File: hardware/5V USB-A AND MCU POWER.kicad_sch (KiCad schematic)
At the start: 19 parts, among them U2 LMR14050-Q1, U3 NCP177BMX330TCG, U4 NCP177AMX120TCG

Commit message: making hardware progress
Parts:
- added R9: 1.5mR, symbol Device:R
- renumbered C13 to C10, C12 to C11, C14 to C12, C15 to C13, C10 to C14, C11 to C15, C18 to C16, C16 to C17, C19 to C18, C17 to C19, R12 to R11, R8 to R12, R9 to R13, U4 to U3, U3 to U4
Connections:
- net +5V: now also R9.2; no longer C15.1, L2.2, R13.2
- new net 5V_CSN: C15.1, L2.2, R13.2, R9.1

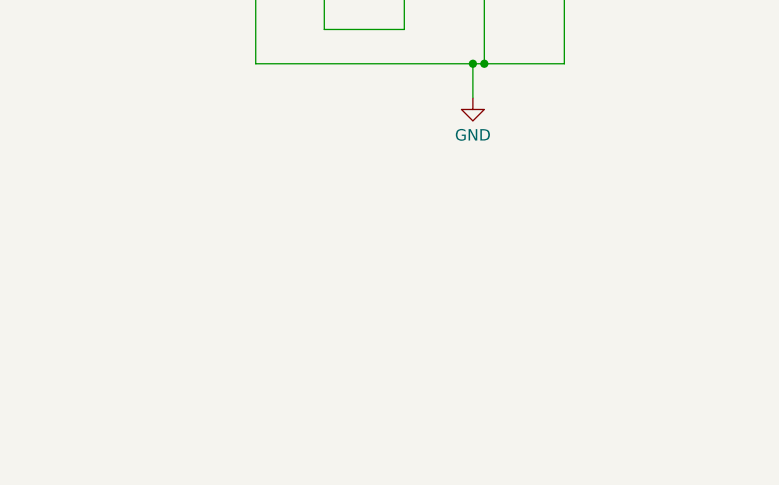
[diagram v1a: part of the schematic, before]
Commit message: working on usb side implimentaion
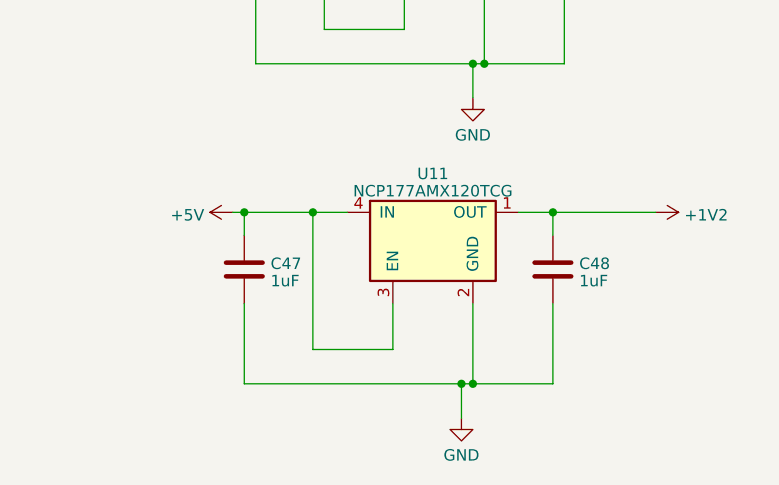
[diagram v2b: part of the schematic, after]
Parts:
- added C47, C48: 1uF, symbol Device:C
- added U11: NCP177AMX120TCG, symbol CARTHING:NCP177BMX330TCG-Regulator_Linear
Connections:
- net +1V2: now also C48.1, U11.1 (OUT)
- net +5V: now also C47.1, U11.3 (EN), U11.4 (IN)
- net GND: now also C47.2, C48.2, U11.2 (GND)
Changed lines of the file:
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@@
   (junction (at 218.44 72.39) (diameter 0) (color 0 0 0 0)
   )
+  (junction (at 182.88 107.95) (diameter 0) (color 0 0 0 0)
+  )
   (junction (at 77.47 88.9) (diameter 0) (color 0 0 0 0)
   )
@@
   (junction (at 135.89 68.58) (diameter 0) (color 0 0 0 0)
   )
+  (junction (at 190.5 107.95) (diameter 0) (color 0 0 0 0)
+  )
   (junction (at 77.47 34.29) (diameter 0) (color 0 0 0 0)
   )
@@
   (junction (at 209.55 91.44) (diameter 0) (color 0 0 0 0)
   )
+  (junction (at 208.28 127) (diameter 0) (color 0 0 0 0)
+  )
+  (junction (at 207.01 127) (diameter 0) (color 0 0 0 0)
+  )
+  (junction (at 217.17 107.95) (diameter 0) (color 0 0 0 0)
+  )
   (junction (at 185.42 31.75) (diameter 0) (color 0 0 0 0)
   )
@@
     (stroke (width 0) (type default))
   )
+  (wire (pts (xy 217.17 107.95) (xy 228.6 107.95))
+    (stroke (width 0) (type default))
+  )
   (wire (pts (xy 77.47 88.9) (xy 77.47 91.44))
     (stroke (width 0) (type default))
@@
     (stroke (width 0) (type default))
   )
+  (wire (pts (xy 190.5 107.95) (xy 194.31 107.95))
+    (stroke (width 0) (type default))
+  )
   (wire (pts (xy 77.47 88.9) (xy 85.09 88.9))
     (stroke (width 0) (type default))
@@
     (stroke (width 0) (type default))
   )
+  (wire (pts (xy 199.39 123.19) (xy 190.5 123.19))
+    (stroke (width 0) (type default))
+  )
   (wire (pts (xy 49.53 88.9) (xy 62.23 88.9))
     (stroke (width 0) (type default))
@@
     (stroke (width 0) (type default))
   )
+  (wire (pts (xy 190.5 123.19) (xy 190.5 107.95))
+    (stroke (width 0) (type default))
+  )
   (wire (pts (xy 110.49 80.01) (xy 110.49 82.55))
     (stroke (width 0) (type default))
@@
     (stroke (width 0) (type default))
   )
+  (wire (pts (xy 199.39 118.11) (xy 199.39 123.19))
+    (stroke (width 0) (type default))
+  )
   (wire (pts (xy 185.42 50.8) (xy 209.55 50.8))
     (stroke (width 0) (type default))
   )
+  (wire (pts (xy 208.28 127) (xy 207.01 127))
+    (stroke (width 0) (type default))
+  )
+  (wire (pts (xy 217.17 118.11) (xy 217.17 127))
+    (stroke (width 0) (type default))
+  )
+  (wire (pts (xy 217.17 107.95) (xy 217.17 110.49))
+    (stroke (width 0) (type default))
+  )
   (wire (pts (xy 102.87 80.01) (xy 110.49 80.01))
     (stroke (width 0) (type default))
@@
     (stroke (width 0) (type default))
   )
+  (wire (pts (xy 181.61 107.95) (xy 182.88 107.95))
+    (stroke (width 0) (type default))
+  )
   (wire (pts (xy 193.04 31.75) (xy 196.85 31.75))
     (stroke (width 0) (type default))
@@
     (stroke (width 0) (type default))
   )
+  (wire (pts (xy 208.28 118.11) (xy 208.28 127))
+    (stroke (width 0) (type default))
+  )
   (wire (pts (xy 77.47 50.8) (xy 76.2 50.8))
     (stroke (width 0) (type default))
@@
     (stroke (width 0) (type default))
   )
+  (wire (pts (xy 182.88 127) (xy 207.01 127))
+    (stroke (width 0) (type default))
+  )
   (wire (pts (xy 184.15 31.75) (xy 185.42 31.75))
     (stroke (width 0) (type default))
@@
     (stroke (width 0) (type default))
   )
+  (wire (pts (xy 217.17 127) (xy 208.28 127))
+    (stroke (width 0) (type default))
+  )
   (wire (pts (xy 49.53 64.77) (xy 49.53 68.58))
     (stroke (width 0) (type default))
@@
     (stroke (width 0) (type default))
   )
+  (wire (pts (xy 213.36 107.95) (xy 217.17 107.95))
+    (stroke (width 0) (type default))
+  )
   (wire (pts (xy 218.44 72.39) (xy 229.87 72.39))
     (stroke (width 0) (type default))
@@
     (stroke (width 0) (type default))
   )
+  (wire (pts (xy 182.88 107.95) (xy 182.88 110.49))
+    (stroke (width 0) (type default))
+  )
   (wire (pts (xy 96.52 45.72) (xy 96.52 44.45))
     (stroke (width 0) (type default))
@@
     (stroke (width 0) (type default))
   )
+  (wire (pts (xy 207.01 127) (xy 207.01 130.81))
+    (stroke (width 0) (type default))
+  )
   (wire (pts (xy 102.87 78.74) (xy 102.87 80.01))
     (stroke (width 0) (type default))
   )
+  (wire (pts (xy 182.88 127) (xy 182.88 118.11))
+    (stroke (width 0) (type default))
+  )
   (wire (pts (xy 219.71 41.91) (xy 219.71 50.8))
     (stroke (width 0) (type default))
@@
   )
   (wire (pts (xy 120.65 68.58) (xy 120.65 71.12))
+    (stroke (width 0) (type default))
+  )
+  (wire (pts (xy 182.88 107.95) (xy 190.5 107.95))
     (stroke (width 0) (type default))
   )
@@
     )
   )
+  (symbol (lib_id "power:+5V") (at 181.61 107.95 90) (unit 1)
+    (in_bom yes) (on_board yes) (dnp no) (fields_autoplaced)
+    (property "Reference" "#PWR056" (at 185.42 107.95 0)
+      (effects (font (size 1.27 1.27)) hide)
+    )
+    (property "Value" "+5V" (at 178.4351 108.2668 90)
+      (effects (font (size 1.27 1.27)) (justify left))
+    )
+    (property "Footprint" "" (at 181.61 107.95 0)
+      (effects (font (size 1.27 1.27)) hide)
+    )
+    (property "Datasheet" "" (at 181.61 107.95 0)
+      (effects (font (size 1.27 1.27)) hide)
+    )
+    (pin "1")
+    (instances
+      (project "usbc-car-module"
+        (path "/fae025e9-99c5-40c1-af6f-99dc1edbfa43/babd34fb-a18a-4bce-9735-4ab8ec7cd7ca"
+          (reference "#PWR056") (unit 1)
+        )
+      )
+    )
+  )
+  (symbol (lib_id "power:GND") (at 207.01 130.81 0) (unit 1)
+    (in_bom yes) (on_board yes) (dnp no) (fields_autoplaced)
+    (property "Reference" "#PWR057" (at 207.01 137.16 0)
+      (effects (font (size 1.27 1.27)) hide)
+    )
+    (property "Value" "GND" (at 207.01 134.9455 0)
+      (effects (font (size 1.27 1.27)))
+    )
+    (property "Footprint" "" (at 207.01 130.81 0)
+      (effects (font (size 1.27 1.27)) hide)
+    )
+    (property "Datasheet" "" (at 207.01 130.81 0)
+      (effects (font (size 1.27 1.27)) hide)
+    )
+    (pin "1")
+    (instances
+      (project "usbc-car-module"
+        (path "/fae025e9-99c5-40c1-af6f-99dc1edbfa43/babd34fb-a18a-4bce-9735-4ab8ec7cd7ca"
+          (reference "#PWR057") (unit 1)
+        )
+      )
+    )
+  )
   (symbol (lib_id "Device:C") (at 218.44 78.74 0) (unit 1)
     (in_bom yes) (on_board yes) (dnp no) (fields_autoplaced)
@@
         (path "/fae025e9-99c5-40c1-af6f-99dc1edbfa43/babd34fb-a18a-4bce-9735-4ab8ec7cd7ca"
           (reference "C14") (unit 1)
+        )
+      )
+    )
+  )
+  (symbol (lib_id "Device:C") (at 217.17 114.3 0) (unit 1)
+    (in_bom yes) (on_board yes) (dnp no) (fields_autoplaced)
+    (property "Reference" "C48" (at 220.091 113.6563 0)
+      (effects (font (size 1.27 1.27)) (justify left))
+    )
+    (property "Value" "1uF" (at 220.091 115.5773 0)
+      (effects (font (size 1.27 1.27)) (justify left))
+    )
+    (property "Footprint" "" (at 218.1352 118.11 0)
+      (effects (font (size 1.27 1.27)) hide)
+    )
+    (property "Datasheet" "~" (at 217.17 114.3 0)
+      (effects (font (size 1.27 1.27)) hide)
+    )
+    (pin "1")
+    (pin "2")
+    (instances
+      (project "usbc-car-module"
+        (path "/fae025e9-99c5-40c1-af6f-99dc1edbfa43/babd34fb-a18a-4bce-9735-4ab8ec7cd7ca"
+          (reference "C48") (unit 1)
         )
       )
@@
     )
   )
+  (symbol (lib_id "Device:C") (at 182.88 114.3 0) (unit 1)
+    (in_bom yes) (on_board yes) (dnp no) (fields_autoplaced)
+    (property "Reference" "C47" (at 185.801 113.6563 0)
+      (effects (font (size 1.27 1.27)) (justify left))
+    )
+    (property "Value" "1uF" (at 185.801 115.5773 0)
+      (effects (font (size 1.27 1.27)) (justify left))
+    )
+    (property "Footprint" "" (at 183.8452 118.11 0)
+      (effects (font (size 1.27 1.27)) hide)
+    )
+    (property "Datasheet" "~" (at 182.88 114.3 0)
+      (effects (font (size 1.27 1.27)) hide)
+    )
+    (pin "1")
+    (pin "2")
+    (instances
+      (project "usbc-car-module"
+        (path "/fae025e9-99c5-40c1-af6f-99dc1edbfa43/babd34fb-a18a-4bce-9735-4ab8ec7cd7ca"
+          (reference "C47") (unit 1)
+        )
+      )
+    )
+  )
   (symbol (lib_id "Device:C") (at 62.23 82.55 0) (unit 1)
     (in_bom yes) (on_board yes) (dnp no) (fields_autoplaced)
@@
         (path "/fae025e9-99c5-40c1-af6f-99dc1edbfa43/babd34fb-a18a-4bce-9735-4ab8ec7cd7ca"
           (reference "C16") (unit 1)
+        )
+      )
+    )
+  )
+  (symbol (lib_id "power:+1V2") (at 228.6 107.95 270) (unit 1)
+    (in_bom yes) (on_board yes) (dnp no) (fields_autoplaced)
+    (property "Reference" "#PWR058" (at 224.79 107.95 0)
+      (effects (font (size 1.27 1.27)) hide)
+    )
+    (property "Value" "+1V2" (at 231.775 108.2668 90)
+      (effects (font (size 1.27 1.27)) (justify left))
+    )
+    (property "Footprint" "" (at 228.6 107.95 0)
+      (effects (font (size 1.27 1.27)) hide)
+    )
+    (property "Datasheet" "" (at 228.6 107.95 0)
+      (effects (font (size 1.27 1.27)) hide)
+    )
+    (pin "1")
+    (instances
+      (project "usbc-car-module"
+        (path "/fae025e9-99c5-40c1-af6f-99dc1edbfa43/babd34fb-a18a-4bce-9735-4ab8ec7cd7ca"
+          (reference "#PWR058") (unit 1)
         )
       )
@@
         )
       )
+    )
+  )
+  (symbol (lib_id "CARTHING:NCP177BMX330TCG-Regulator_Linear") (at 201.93 110.49 0) (unit 1)
+    (in_bom yes) (on_board yes) (dnp no) (fields_autoplaced)
+    (property "Reference" "U11" (at 203.835 103.6701 0)
+      (effects (font (size 1.27 1.27)))
+    )
+    (property "Value" "NCP177AMX120TCG" (at 203.835 105.5911 0)
+      (effects (font (size 1.27 1.27)))
+    )
+    (property "Footprint" "" (at 203.2 101.6 0)
+      (effects (font (size 1.27 1.27)) hide)
+    )
+    (property "Datasheet" "" (at 203.2 101.6 0)
+      (effects (font (size 1.27 1.27)) hide)
+    )
+    (pin "1")
+    (pin "2")
+    (pin "3")
+    (pin "4")
+    (instances
+      (project "usbc-car-module"
+        (path "/fae025e9-99c5-40c1-af6f-99dc1edbfa43/babd34fb-a18a-4bce-9735-4ab8ec7cd7ca"
+          (reference "U11") (unit 1)
+        )
+      )

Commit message: finnished rudimentry schimatics still needs alot of work
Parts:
- added D22: LED, symbol Device:LED
- added R97: 500R, symbol Device:R
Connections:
- net +21V: now also U2.4 (EN)
- net +5V: now also D22.2 (A), R97.1
- net at U2.8 (PGOOD): now also D22.1 (K), R97.2
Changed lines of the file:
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@@
   (junction (at 62.23 88.9) (diameter 0) (color 0 0 0 0)
   )
+  (junction (at 41.91 52.07) (diameter 0) (color 0 0 0 0)
+  )
   (junction (at 120.65 68.58) (diameter 0) (color 0 0 0 0)
   )
@@
   (junction (at 184.15 72.39) (diameter 0) (color 0 0 0 0)
   )
+  (junction (at 77.47 46.99) (diameter 0) (color 0 0 0 0)
+  )
   (wire (pts (xy 85.09 34.29) (xy 85.09 36.83))
     (stroke (width 0) (type default))
@@
     (stroke (width 0) (type default))
   )
+  (wire (pts (xy 41.91 52.07) (xy 63.5 52.07))
+    (stroke (width 0) (type default))
+  )
   (wire (pts (xy 184.15 72.39) (xy 191.77 72.39))
     (stroke (width 0) (type default))
@@
     (stroke (width 0) (type default))
   )
+  (wire (pts (xy 64.77 46.99) (xy 77.47 46.99))
+    (stroke (width 0) (type default))
+  )
+  (wire (pts (xy 63.5 52.07) (xy 63.5 63.5))
+    (stroke (width 0) (type default))
+  )
   (wire (pts (xy 209.55 91.44) (xy 208.28 91.44))
     (stroke (width 0) (type default))
@@
     (stroke (width 0) (type default))
   )
+  (wire (pts (xy 77.47 46.99) (xy 77.47 50.8))
+    (stroke (width 0) (type default))
+  )
   (wire (pts (xy 201.93 41.91) (xy 201.93 46.99))
     (stroke (width 0) (type default))
   )
+  (wire (pts (xy 64.77 60.96) (xy 64.77 46.99))
+    (stroke (width 0) (type default))
+  )
   (wire (pts (xy 77.47 31.75) (xy 77.47 34.29))
     (stroke (width 0) (type default))
@@
     (stroke (width 0) (type default))
   )
+  (wire (pts (xy 41.91 41.91) (xy 41.91 43.18))
+    (stroke (width 0) (type default))
+  )
   (wire (pts (xy 217.17 127) (xy 208.28 127))
     (stroke (width 0) (type default))
@@
     (stroke (width 0) (type default))
   )
-  (wire (pts (xy 77.47 34.29) (xy 77.47 50.8))
+  (wire (pts (xy 36.83 52.07) (xy 41.91 52.07))
+    (stroke (width 0) (type default))
+  )
+  (wire (pts (xy 77.47 34.29) (xy 77.47 46.99))
     (stroke (width 0) (type default))
   )
@@
     (stroke (width 0) (type default))
   )
+  (wire (pts (xy 27.94 52.07) (xy 29.21 52.07))
+    (stroke (width 0) (type default))
+  )
   (wire (pts (xy 120.65 68.58) (xy 132.08 68.58))
     (stroke (width 0) (type default))
@@
     (stroke (width 0) (type default))
   )
+  (wire (pts (xy 41.91 50.8) (xy 41.91 52.07))
+    (stroke (width 0) (type default))
+  )
   (wire (pts (xy 87.63 60.96) (xy 92.71 60.96))
     (stroke (width 0) (type default))
@@
     (stroke (width 0) (type default))
   )
+  (wire (pts (xy 63.5 63.5) (xy 67.31 63.5))
+    (stroke (width 0) (type default))
+  )
   (wire (pts (xy 218.44 72.39) (xy 229.87 72.39))
     (stroke (width 0) (type default))
@@
   )
   (wire (pts (xy 120.65 68.58) (xy 120.65 71.12))
+    (stroke (width 0) (type default))
+  )
+  (wire (pts (xy 67.31 60.96) (xy 64.77 60.96))
     (stroke (width 0) (type default))
   )
@@
     )
   )
+  (symbol (lib_id "Device:LED") (at 33.02 52.07 180) (unit 1)
+    (in_bom yes) (on_board yes) (dnp no) (fields_autoplaced)
+    (property "Reference" "D22" (at 34.6075 46.9011 0)
+      (effects (font (size 1.27 1.27)))
+    )
+    (property "Value" "LED" (at 34.6075 48.8221 0)
+      (effects (font (size 1.27 1.27)))
+    )
+    (property "Footprint" "" (at 33.02 52.07 0)
+      (effects (font (size 1.27 1.27)) hide)
+    )
+    (property "Datasheet" "~" (at 33.02 52.07 0)
+      (effects (font (size 1.27 1.27)) hide)
+    )
+    (pin "1")
+    (pin "2")
+    (instances
+      (project "usbc-car-module"
+        (path "/fae025e9-99c5-40c1-af6f-99dc1edbfa43/babd34fb-a18a-4bce-9735-4ab8ec7cd7ca"
+          (reference "D22") (unit 1)
+        )
+      )
+    )
+  )
   (symbol (lib_id "Device:C_Polarized_US") (at 120.65 74.93 0) (unit 1)
     (in_bom yes) (on_board yes) (dnp no) (fields_autoplaced)
@@
         (path "/fae025e9-99c5-40c1-af6f-99dc1edbfa43/babd34fb-a18a-4bce-9735-4ab8ec7cd7ca"
           (reference "#PWR015") (unit 1)
+        )
+      )
+    )
+  )
+  (symbol (lib_id "power:+5V") (at 27.94 52.07 90) (unit 1)
+    (in_bom yes) (on_board yes) (dnp no) (fields_autoplaced)
+    (property "Reference" "#PWR0127" (at 31.75 52.07 0)
+      (effects (font (size 1.27 1.27)) hide)
+    )
+    (property "Value" "+5V" (at 24.7651 52.3868 90)
+      (effects (font (size 1.27 1.27)) (justify left))
+    )
+    (property "Footprint" "" (at 27.94 52.07 0)
+      (effects (font (size 1.27 1.27)) hide)
+    )
+    (property "Datasheet" "" (at 27.94 52.07 0)
+      (effects (font (size 1.27 1.27)) hide)
+    )
+    (pin "1")
+    (instances
+      (project "usbc-car-module"
+        (path "/fae025e9-99c5-40c1-af6f-99dc1edbfa43/babd34fb-a18a-4bce-9735-4ab8ec7cd7ca"
+          (reference "#PWR0127") (unit 1)
         )
       )
@@
     )
   )
+  (symbol (lib_id "Device:R") (at 41.91 46.99 0) (unit 1)
+    (in_bom yes) (on_board yes) (dnp no) (fields_autoplaced)
+    (property "Reference" "R97" (at 43.688 46.3463 0)
+      (effects (font (size 1.27 1.27)) (justify left))
+    )
+    (property "Value" "500R" (at 43.688 48.2673 0)
+      (effects (font (size 1.27 1.27)) (justify left))
+    )
+    (property "Footprint" "" (at 40.132 46.99 90)
+      (effects (font (size 1.27 1.27)) hide)
+    )
+    (property "Datasheet" "~" (at 41.91 46.99 0)
+      (effects (font (size 1.27 1.27)) hide)
+    )
+    (pin "1")
+    (pin "2")
+    (instances
+      (project "usbc-car-module"
+        (path "/fae025e9-99c5-40c1-af6f-99dc1edbfa43/babd34fb-a18a-4bce-9735-4ab8ec7cd7ca"
+          (reference "R97") (unit 1)
+        )
+      )
+    )
+  )
   (symbol (lib_id "power:+5V") (at 181.61 107.95 90) (unit 1)
     (in_bom yes) (on_board yes) (dnp no) (fields_autoplaced)
@@
         )
       )
+    )
+  )
+  (symbol (lib_id "power:+5V") (at 41.91 41.91 0) (unit 1)
+    (in_bom yes) (on_board yes) (dnp no) (fields_autoplaced)
+    (property "Reference" "#PWR0128" (at 41.91 45.72 0)
+      (effects (font (size 1.27 1.27)) hide)
+    )
+    (property "Value" "+5V" (at 41.91 38.4081 0)
+      (effects (font (size 1.27 1.27)))
+    )
+    (property "Footprint" "" (at 41.91 41.91 0)
+      (effects (font (size 1.27 1.27)) hide)
+    )
+    (property "Datasheet" "" (at 41.91 41.91 0)
+      (effects (font (size 1.27 1.27)) hide)
+    )
+    (pin "1")
+    (instances
+      (project "usbc-car-module"
+        (path "/fae025e9-99c5-40c1-af6f-99dc1edbfa43/babd34fb-a18a-4bce-9735-4ab8ec7cd7ca"
+          (reference "#PWR0128") (unit 1)
+        )
+      )

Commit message: working on hardware
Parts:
- added C10, C14: 1uF, Capacitor_SMD:C_0603_1608Metric, symbol Device:C
- added U2: NCP177BMX330TCG, CARTHING:VREG_NCP170AMX300TCG, symbol CARTHING:NCP177BMX330TCG-Regulator_Linear
- C11: renamed from C17; footprint (none) -> Capacitor_SMD:C_0603_1608Metric
- C12: renamed from C10; footprint (none) -> Capacitor_SMD:C_0603_1608Metric
- C13: renamed from C11; footprint (none) -> Capacitor_SMD:C_0603_1608Metric
- C15: renamed from C19; footprint (none) -> Capacitor_SMD:C_0603_1608Metric
- C16: renamed from C12; footprint (none) -> Capacitor_SMD:C_0603_1608Metric
- C17: renamed from C13; footprint (none) -> Capacitor_SMD:C_0603_1608Metric
- C18: renamed from C14; footprint (none) -> Capacitor_SMD:C_0603_1608Metric
- C19: renamed from C16; footprint (none) -> Capacitor_SMD:C_0603_1608Metric
- C20: renamed from C47; footprint (none) -> Capacitor_SMD:C_0603_1608Metric
- C21: renamed from C15; footprint (none) -> Capacitor_SMD:C_1210_3225Metric
- C22: renamed from C18; footprint (none) -> Capacitor_SMD:C_0603_1608Metric
- C23: renamed from C48; footprint (none) -> Capacitor_SMD:C_0603_1608Metric
- D1: renamed from D22; footprint (none) -> Diode_SMD:D_0603_1608Metric
- D2: renamed from D1; footprint (none) -> Diode_SMD:D_SMA
- U3: renamed from U4; footprint (none) -> CARTHING:VREG_NCP170AMX300TCG
- U5: renamed from U3; footprint (none) -> CARTHING:VREG_NCP170AMX300TCG
- U6: renamed from U11; footprint (none) -> CARTHING:VREG_NCP170AMX300TCG
- renumbered R97 to R11, R10 to R12, R11 to R13, R12 to R14, R13 to R15, U2 to U4
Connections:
- net +3V3: now also C14.1, U2.1 (OUT)
- net +5V: now also C10.1, U2.3 (EN), U2.4 (IN)
- net GND: now also C10.2, C14.2, U2.2 (GND)
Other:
- note added: "1V2 SUPPLY"
- note added: "3V3 SUPPLY"
- note added: "5V SUPPLY"
- moved on the sheet: C11, C15, C19, C20, C22, C23, U3, U5, U6
